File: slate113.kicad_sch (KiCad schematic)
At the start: 59 parts, among them J1 TYPE-C16PIN, J2 TYPE-C16PIN, J3 Conn_01x06_Pin, J4 DF40C-100DP-0.4V51, J5 DF40C-100DP-0.4V51, Q5 CSD17575Q3A, Q6 CSD17575Q3A, Q7 CSD17575Q3A, Q8 CSD17575Q3A, SW1 RESET_L, SW2 PWRON_L, U1 FUSB302BMPX, U2 CH224K, U3 BQ25792RQMR, U4 AP2112K-3.3TRG1, U5 AP2112K-1.8TRG1, U6 LP8556SQ-E09/NOPB, U7 USBLC6-2P6, U8 ESD7104MUTAG_C2987068, U9 TPS61088RHLR

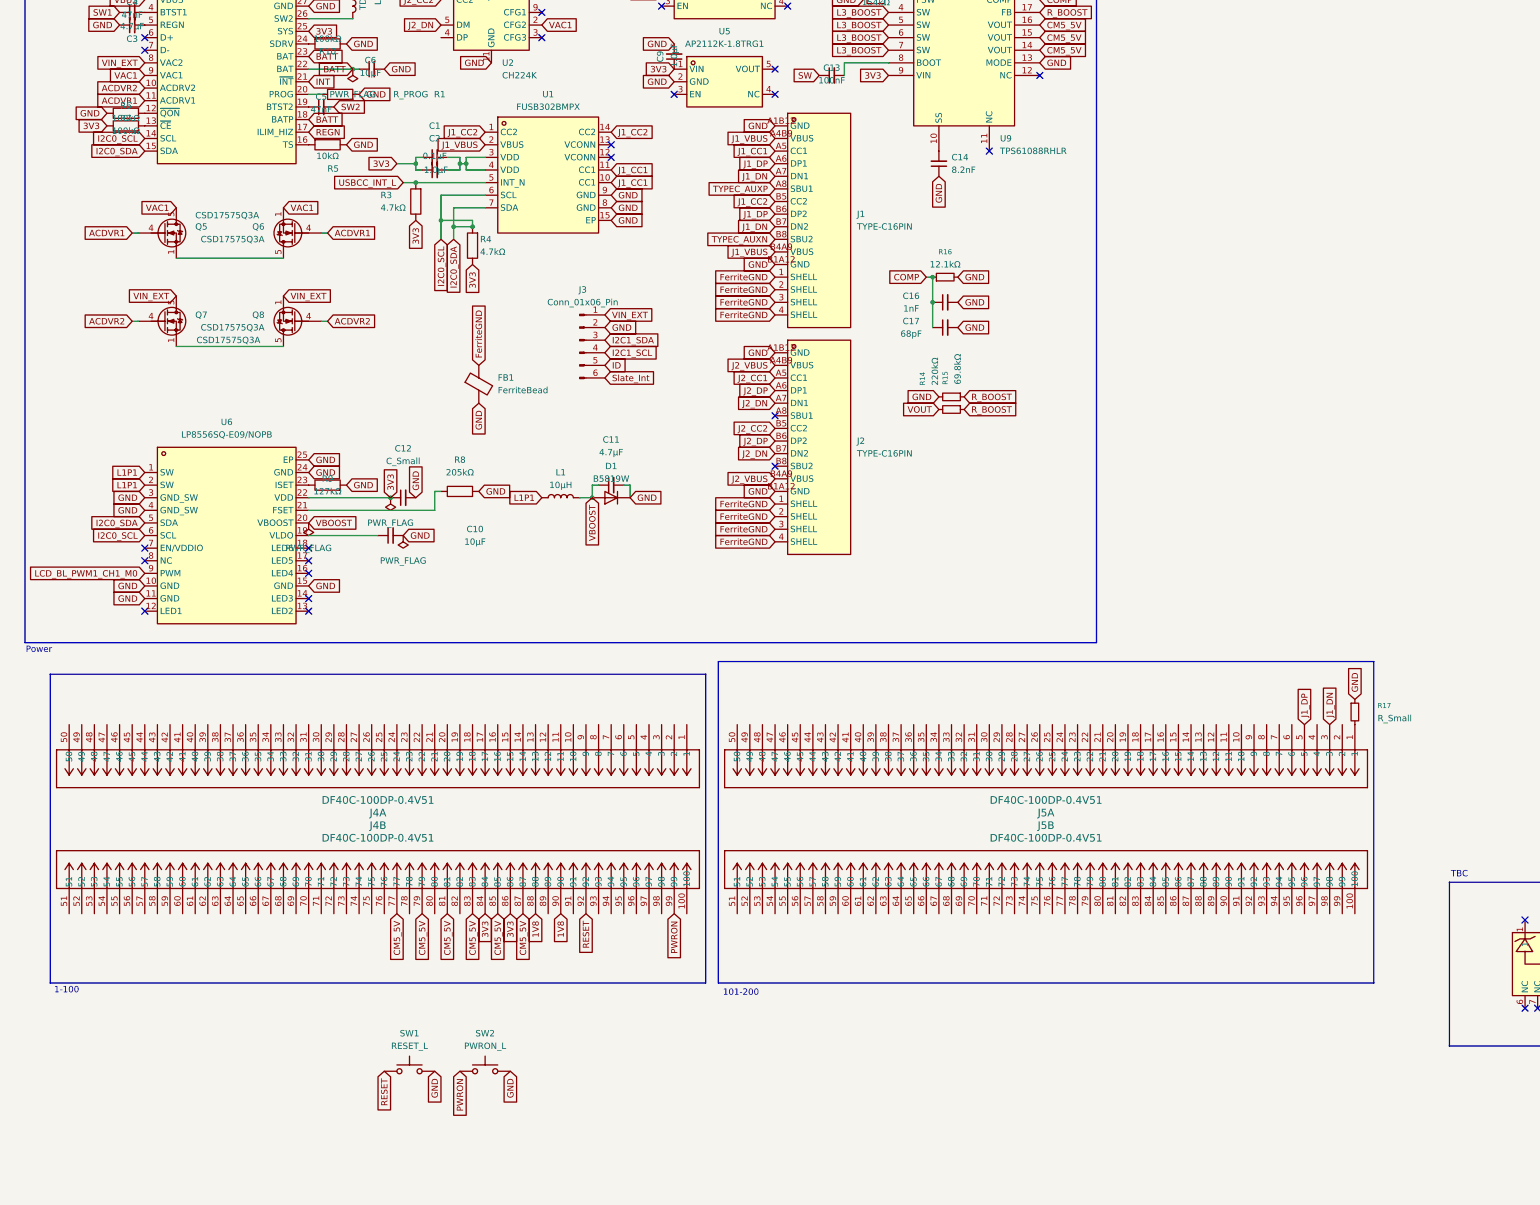
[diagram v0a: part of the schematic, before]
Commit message: Continue wiring up CM5 Conector, as well as USB A, Micro SD, and M.2 B.Key Slot, with the B-Key being partially done.
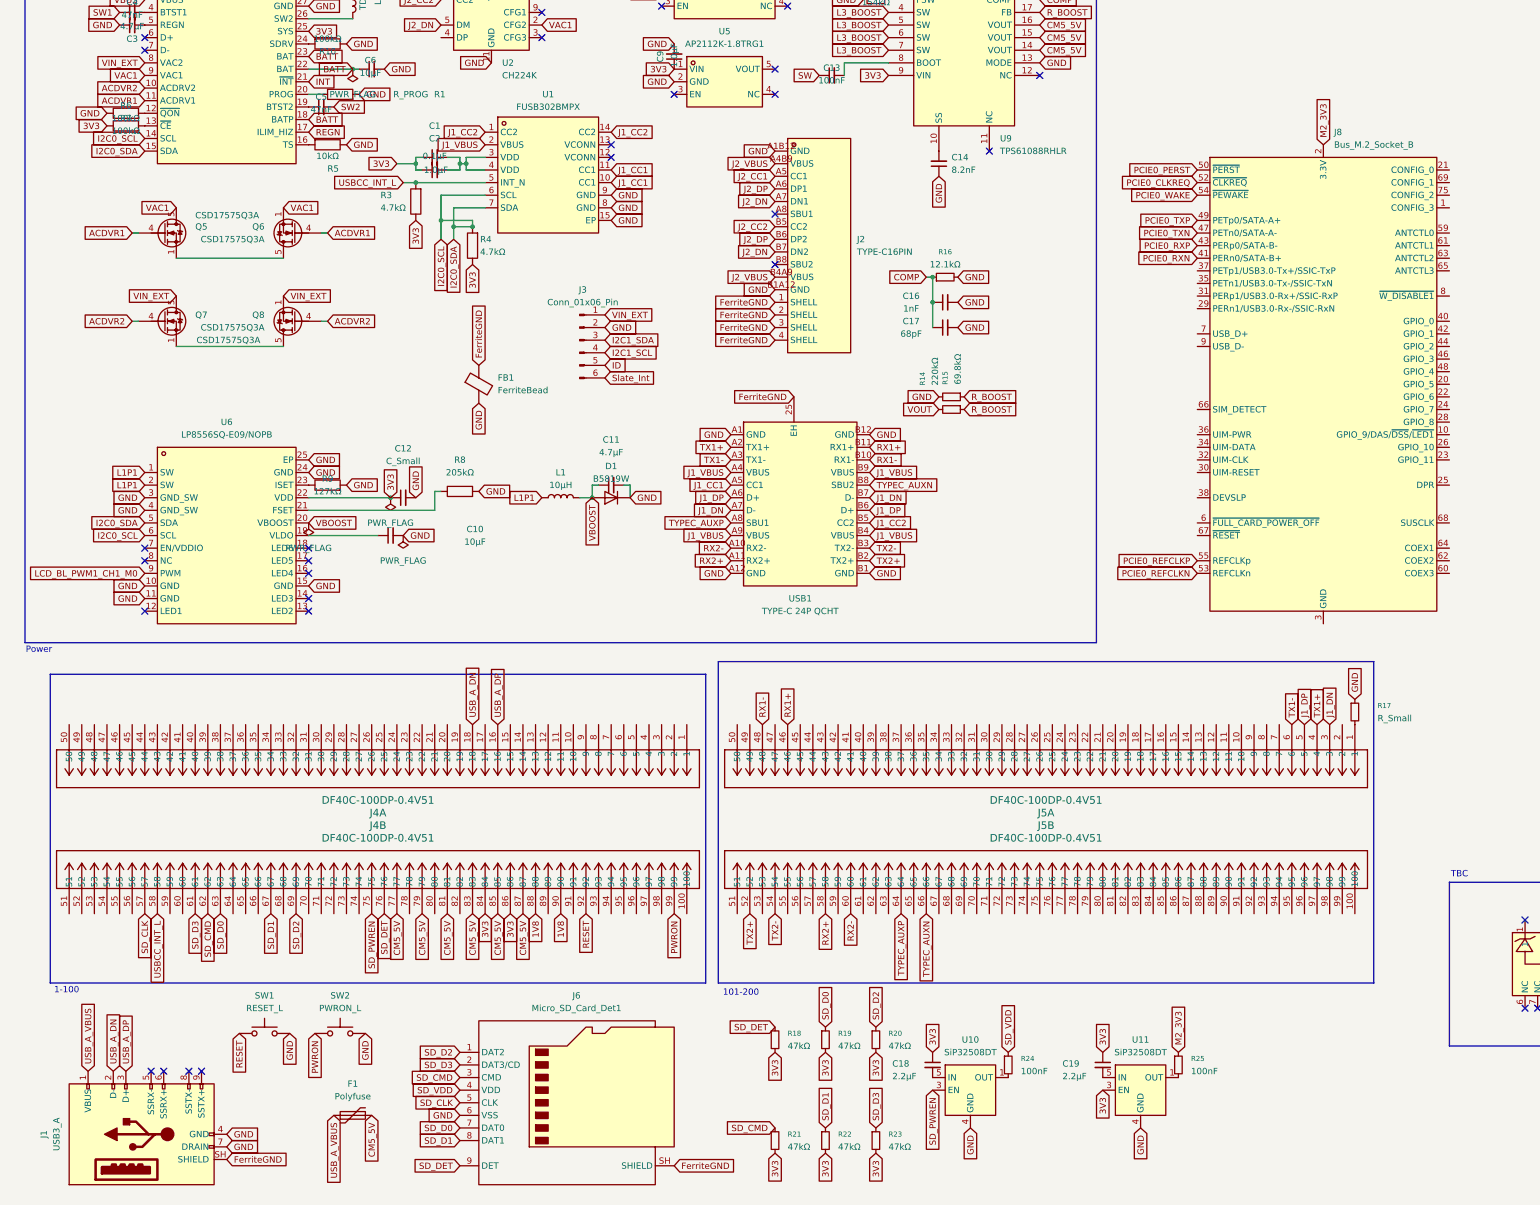
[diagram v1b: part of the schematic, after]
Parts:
- removed J1: TYPE-C16PIN, slate113:USB-C-SMD_TYPE-C16PIN, symbol slate113:TYPE-C16PIN
- added C18, C19: 2.2µF, symbol Device:C_Small
- added F1: Polyfuse, symbol Device:Polyfuse
- added J1: USB3_A, symbol Connector:USB3_A
- added J6: Micro_SD_Card_Det1, symbol Connector:Micro_SD_Card_Det1
- added J8: Bus_M.2_Socket_B, symbol Connector:Bus_M.2_Socket_B
- added R18, R19, R20, R21, R22, R23: 47kΩ, symbol Device:R_Small
- added R24, R25: 100nF, symbol Device:R_Small
- added U10, U11: SiP32508DT, Package_TO_SOT_SMD:TSOT-23-6, symbol Power_Management:SiP32508DT
- added USB1: TYPE-C 24P QCHT, slate113:TYPE-C-SMD_TYPE-C-24P-QCHT, symbol slate113:TYPE-C24PQCHT
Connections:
- net 3V3: now also C18.1, C19.1, R18.2, R19.2, R20.2, R21.2, R22.2, R23.2, U11.3 (EN)
- net CM5_5V: now also F1.2
- net FerriteGND: now also J1.SH (SHIELD), J6.SH (SHIELD), USB1.25 (EH)
- net GND: now also J1.4 (GND), J1.7 (DRAIN), J6.6 (VSS), U10.4 (GND), U11.4 (GND), USB1.A1 (GND), USB1.A12 (GND), USB1.B1 (GND), USB1.B12 (GND)
- net J1_CC1: now also USB1.A5 (CC1)
- net J1_CC2: now also USB1.B5 (CC2)
- net J1_DN: now also USB1.A7 (D-), USB1.B7 (D-)
- net J1_DP: now also USB1.A6 (D+), USB1.B6 (D+)
- net J1_VBUS: now also USB1.A4 (VBUS), USB1.A9 (VBUS), USB1.B4 (VBUS), USB1.B9 (VBUS)
- net TYPEC_AUXN: now also J5.66, USB1.B8 (SBU2)
- net TYPEC_AUXP: now also J5.64, USB1.A8 (SBU1)
- net USBCC_INT_L: now also J4.58
- net TX1+: now reaches J5.4
- net TX1+: now also USB1.A2 (TX1+)
- net RX1+: now reaches J5.46
- net RX1+: now also USB1.B11 (RX1+)
- net RX1-: now reaches J5.48
- net RX1-: now also USB1.B10 (RX1-)
- net TX1-: now reaches J5.6
- net TX1-: now also USB1.A3 (TX1-)
- net TX2+: now reaches J5.52
- net TX2+: now also USB1.B2 (TX2+)
- net TX2-: now reaches J5.54
- net TX2-: now also USB1.B3 (TX2-)
- net RX2+: now reaches J5.58
- net RX2+: now also USB1.A11 (RX2+)
- net RX2-: now reaches J5.60
- net RX2-: now also USB1.A10 (RX2-)
- net SD_CLK: now reaches J4.57
- net SD_CLK: now also J6.5 (CLK)
- net SD_D3: now reaches J4.61
- net SD_D3: now also J6.2 (DAT3/CD), R23.1
- net SD_CMD: now reaches J4.62
- net SD_CMD: now also J6.3 (CMD), R21.1
- net SD_D0: now reaches J4.63
- net SD_D0: now also J6.7 (DAT0), R19.1
- net SD_D1: now reaches J4.67
- net SD_D1: now also J6.8 (DAT1), R22.1
- net SD_D2: now reaches J4.69
- net SD_D2: now also J6.1 (DAT2), R20.1
- net SD_PWREN: now reaches J4.75
- net SD_PWREN: now also U10.3 (EN)
- net SD_DET: now reaches J4.76
- net SD_DET: now also J6.9 (DET), R18.1
- net USB_A_DP: now reaches J4.16
- net USB_A_DP: now also J1.3 (D+)
- net USB_A_DN: now reaches J4.18
- net USB_A_DN: now also J1.2 (D-)
- new net: R24.2, U10.1 (OUT), U10.2 (OUT)
- new net: C19.2, U11.5 (IN), U11.6 (IN)
- new net: J8.11 (GND), J8.27 (GND), J8.3 (GND), J8.33 (GND), J8.39 (GND), J8.45 (GND), J8.5 (GND), J8.51 (GND), J8.57 (GND), J8.71 (GND), J8.73 (GND)
- new net: C18.2, U10.5 (IN), U10.6 (IN)
- new net: R25.2, U11.1 (OUT), U11.2 (OUT)
- new net M2_3V3: J8.2 (3.3V), J8.4 (3.3V), J8.70 (3.3V), J8.72 (3.3V), J8.74 (3.3V), R25.1
- new net PCIE0_CLKREQ: J8.52 (~{CLKREQ})
- new net PCIE0_PERST: J8.50 (~{PERST})
- new net PCIE0_REFCLKN: J8.53 (REFCLKn)
- new net PCIE0_REFCLKP: J8.55 (REFCLKp)
- new net PCIE0_RXN: J8.41 (PERn0/SATA-B+)
- new net PCIE0_RXP: J8.43 (PERp0/SATA-B-)
- new net PCIE0_TXN: J8.47 (PETn0/SATA-A-)
- new net PCIE0_TXP: J8.49 (PETp0/SATA-A+)
- new net PCIE0_WAKE: J8.54 (~{PEWAKE})
- new net SD_VDD: J6.4 (VDD), R24.1
- new net USB_A_VBUS: F1.1, J1.1 (VBUS)
- no-connect marks 41 -> 45
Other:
- moved on the sheet: J2, SW1, SW2

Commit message: Finished wiring CM5 connector, separated boards into separate Top Level Schematics, and start wiring up B2B connectors (FPC)
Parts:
- removed C1: 0.1µF, symbol Device:C_Small
- removed C10, C6, C7: 10µF, symbol Device:C_Small
- removed C11, C3: 4.7µF, symbol Device:C_Small
- removed C12: C_Small, symbol Device:C_Small
- removed C13: 100nF, symbol Device:C_Small
- removed C14: 8.2nF, symbol Device:C_Small
- removed C15: 1µF, symbol Device:C_Small
- removed C16: 1nF, symbol Device:C_Small
- removed C17: 68pF, symbol Device:C_Small
- removed C18, C19: 2.2µF, symbol Device:C_Small
- removed C2, C8, C9: 1.0µF, symbol Device:C_Small
- removed C4, C5: 47nF, symbol Device:C_Small
- removed D1: B5819W, symbol Device:D
- removed F1: Polyfuse, symbol Device:Polyfuse
- removed FB1: FerriteBead, symbol Device:FerriteBead
- removed J1: USB3_A, symbol Connector:USB3_A
- removed J2: TYPE-C16PIN, slate113:USB-C-SMD_TYPE-C16PIN, symbol slate113:TYPE-C16PIN
- removed J3: Conn_01x06_Pin, symbol Connector:Conn_01x06_Pin
- removed J4, J5: DF40C-100DP-0.4V51, CONN100_DF40C-100DP-0.4V51_HIR, symbol slate113:DF40C-100DP-0.4V51
- removed J6: Micro_SD_Card_Det1, symbol Connector:Micro_SD_Card_Det1
- removed J8: Bus_M.2_Socket_B, symbol Connector:Bus_M.2_Socket_B
- removed L1: 10µH, symbol Device:L
- removed L2: TDK | SPM6530T-1R0M120 | 1µH, symbol Device:L
- removed L3_BOOST: SPM6530T-1R0M120 | 1µH, symbol Device:L
- removed Q5, Q6, Q7, Q8: CSD17575Q3A, Package_TO_SOT_SMD:TDSON-8-1, symbol Transistor_FET:CSD17570Q5B
- removed R1: R_PROG, symbol Device:R
- removed R10, R6, R7: 100kΩ, symbol Device:R
- removed R11: 100kΩ, symbol Device:R_Small
- removed R12: 154kΩ, symbol Device:R_Small
- removed R13: 174kΩ, symbol Device:R_Small
- removed R14: 220kΩ, symbol Device:R_Small
- removed R15: 69.8kΩ, symbol Device:R_Small
- removed R16: 12.1kΩ, symbol Device:R_Small
- removed R17: R_Small, symbol Device:R_Small
- removed R18, R19, R20, R21, R22, R23: 47kΩ, symbol Device:R_Small
- removed R2, R5: 10kΩ, symbol Device:R
- removed R24, R25: 100nF, symbol Device:R_Small
- removed R3, R4: 4.7kΩ, symbol Device:R
- removed R8: 205kΩ, symbol Device:R
- removed R9: 127kΩ, symbol Device:R
- removed SW1: RESET_L, symbol Switch:SW_Push
- removed SW2: PWRON_L, symbol Switch:SW_Push
- removed U1: FUSB302BMPX, slate113:MLP-14_L2.5-W2.5-P0.50-BL-EP, symbol slate113:FUSB302BMPX
- removed U10, U11: SiP32508DT, Package_TO_SOT_SMD:TSOT-23-6, symbol Power_Management:SiP32508DT
- removed U2: CH224K, Package_SO:SSOP-10-1EP_3.9x4.9mm_P1mm_EP2.1x3.3mm, symbol Interface_USB:CH224K
- removed U3: BQ25792RQMR, slate113:QFN-29_L4.0-W4.0-P0.40-TL-BQ25792RQMR, symbol slate113:BQ25792RQMR
- removed U4: AP2112K-3.3TRG1, slate113:SOT-25-5_L2.9-W1.6-P0.95-LS2.8-BL, symbol slate113:AP2112K-3.3TRG1
- removed U5: AP2112K-1.8TRG1, slate113:SOT-25_L3.0-W1.6-P0.95-LS2.8-BL, symbol slate113:AP2112K-1.8TRG1
- removed U6: LP8556SQ-E09/NOPB, slate113:WQFN-24_L4.0-W4.0-P0.50-BL-EP2.5, symbol slate113:LP8556SQ-E09_NOPB
- removed U7: USBLC6-2P6, Package_TO_SOT_SMD:SOT-666, symbol Power_Protection:USBLC6-2P6
- removed U8: ESD7104MUTAG_C2987068, slate113:DFN-10_L2.5-W1.0-P0.50-BL, symbol slate113:ESD7104MUTAG_C2987068
- removed U9: TPS61088RHLR, slate113:VQFN-20_L4.6-W3.6-P0.50-BL, symbol slate113:TPS61088RHLR
- removed USB1: TYPE-C 24P QCHT, slate113:TYPE-C-SMD_TYPE-C-24P-QCHT, symbol slate113:TYPE-C24PQCHT
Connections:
- no-connect marks 45 -> 0
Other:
- note removed: "1-100"
- note removed: "101-200"
- note removed: "Power"
- note removed: "TBC"
